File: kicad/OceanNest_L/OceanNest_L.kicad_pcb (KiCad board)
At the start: 2 copper layers, 104.5 x 86 mm, 38 parts, among them J1 TRRS_MJ-4PP-9, SW1 SW_PUSH, SW10 SW_PUSH, SW11 SW_PUSH, SW12 SW_PUSH, SW13 SW_PUSH, SW14 SW_PUSH, SW15 SW_PUSH, SW16 SW_PUSH, SW2 SW_PUSH, SW3 SW_PUSH, SW4 SW_PUSH, SW5 SW_PUSH, SW6 SW_PUSH, SW7 SW_PUSH, SW8 SW_PUSH, SW9 SW_PUSH, U1 RP2040-Zero

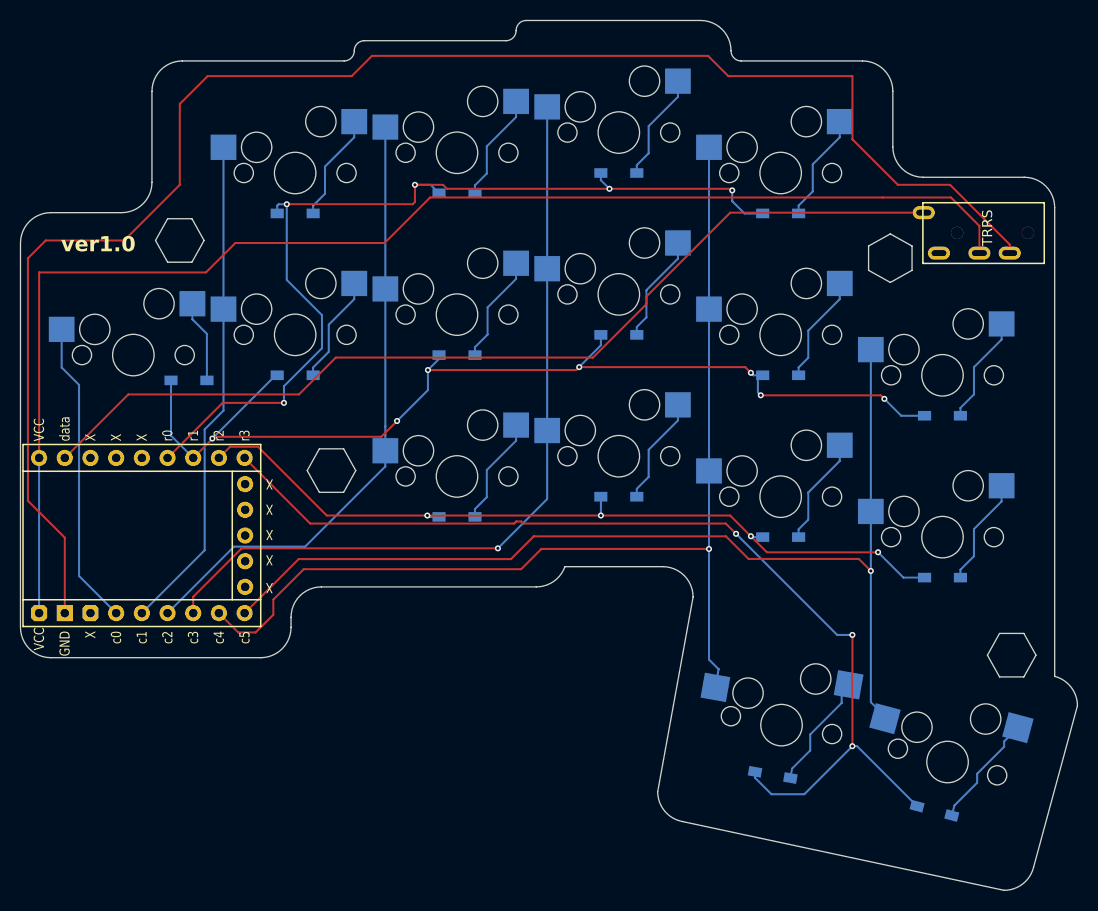
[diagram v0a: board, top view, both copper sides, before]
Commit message: refactor: update PCB properties and footprints for OceanNest project, including footprint layer changes and model path adjustments
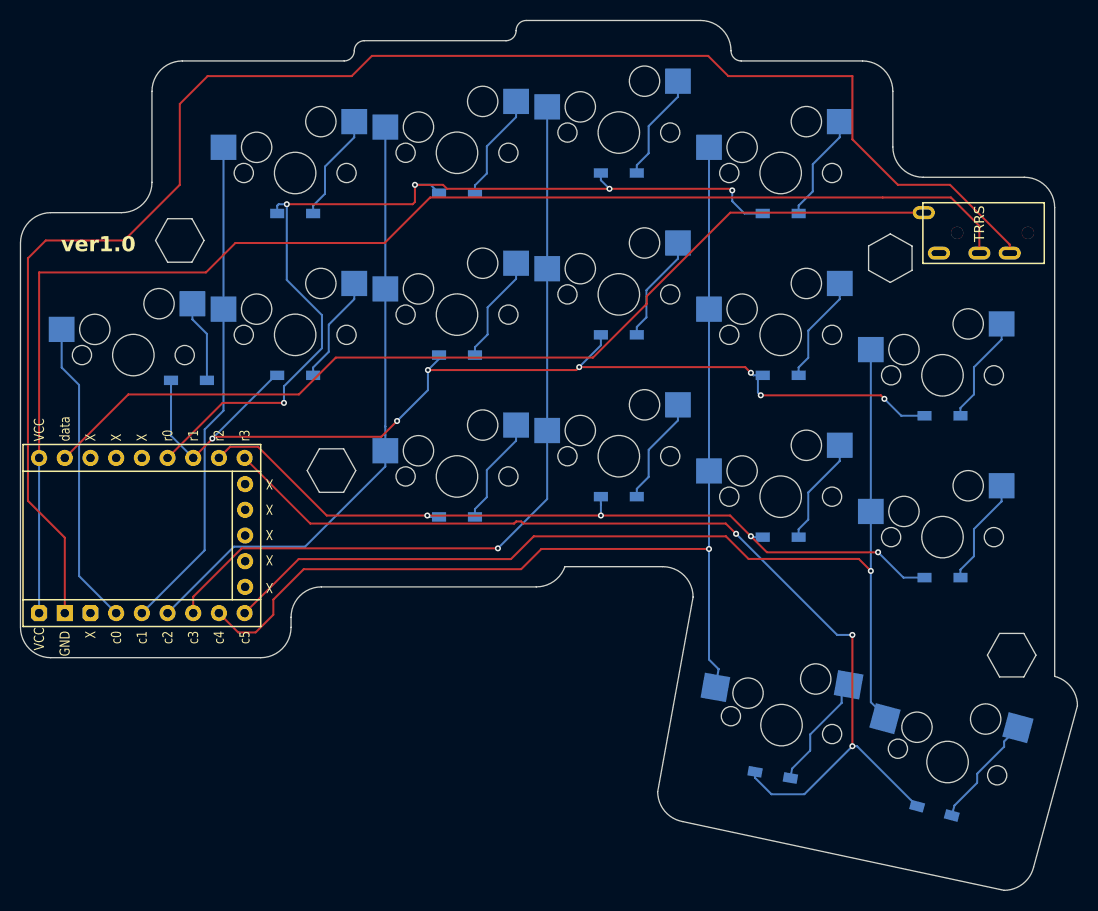
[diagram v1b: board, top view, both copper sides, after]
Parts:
- D1, D10, D11, D12, D13, D14, D15, D16, D2, D3, D4, D5, D6, D7, D8, D9: footprint kbd_Parts:Diode_SMD -> isw-kbd:Diode_SMD
- J1: value TRRS_MJ-4PP-9 -> MJ-4PP-9_BL_kai
